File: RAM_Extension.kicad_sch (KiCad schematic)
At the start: 22 parts, among them J2 EXT, U1 LFE5U-85F-8BG381C, U4 IS66WVE4M16EBLL-70BLI

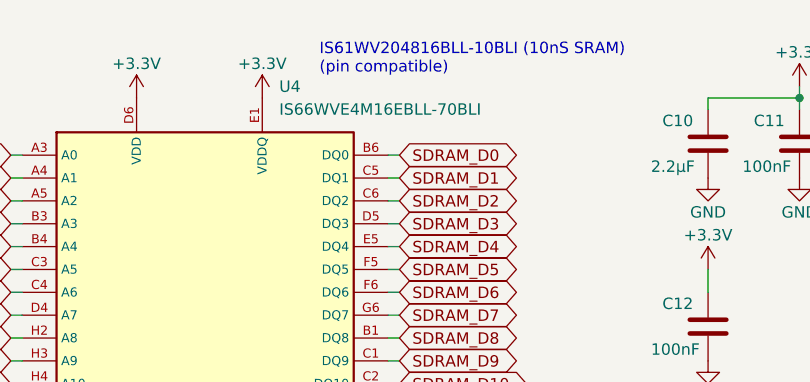
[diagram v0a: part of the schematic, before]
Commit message: Switched to project library
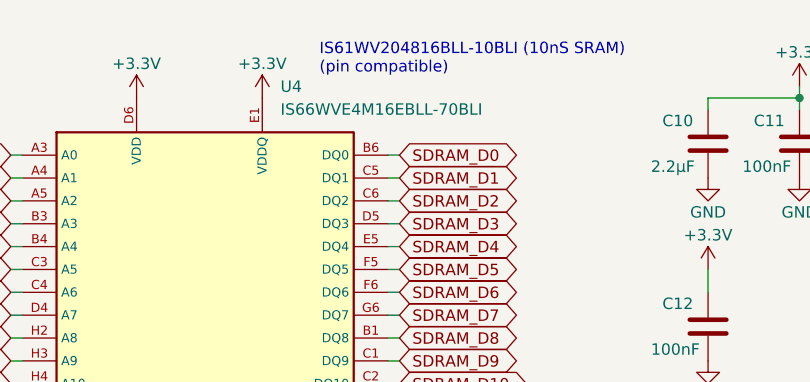
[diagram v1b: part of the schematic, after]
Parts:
- J2: footprint Gil:FTS-120-02-L-DV -> ECP5_RISCV:FTS-120-02-L-DV
- U1: footprint Gil:BGA-381_pitch0.8mm_dia0.4mm -> ECP5_RISCV:BGA-381_pitch0.8mm_dia0.4mm; symbol Gil:LFE5U-85F-6BG381x -> ECP5_RISCV:LFE5U-85F-6BG381x
- U4: footprint Gil:BGA48C75P8X6_800X600X120N -> ECP5_RISCV:BGA48C75P8X6_800X600X120N; symbol Gil:IS66WVE4M16E -> ECP5_RISCV:IS66WVE4M16E

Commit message: Changed the name of the project path to ECP5_BGA381_RISCV
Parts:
- J2: footprint ECP5_RISCV:FTS-120-02-L-DV -> ECP5_BGA381_RISCV:FTS-120-02-L-DV
- U1: footprint ECP5_RISCV:BGA-381_pitch0.8mm_dia0.4mm -> ECP5_BGA381_RISCV:BGA-381_pitch0.8mm_dia0.4mm; symbol ECP5_RISCV:LFE5U-85F-6BG381x -> ECP5_BGA381_RISCV:LFE5U-85F-6BG381x
- U4: footprint ECP5_RISCV:BGA48C75P8X6_800X600X120N -> ECP5_BGA381_RISCV:BGA48C75P8X6_800X600X120N; symbol ECP5_RISCV:IS66WVE4M16E -> ECP5_BGA381_RISCV:IS66WVE4M16E
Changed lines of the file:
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@@
 	)
 	(symbol
-		(lib_id "ECP5_RISCV:LFE5U-85F-6BG381x")
+		(lib_id "ECP5_BGA381_RISCV:LFE5U-85F-6BG381x")
 		(at 74.93 146.05 0)
 		(unit 4)
@@
 			)
 		)
-		(property "Footprint" "ECP5_RISCV:BGA-381_pitch0.8mm_dia0.4mm"
+		(property "Footprint" "ECP5_BGA381_RISCV:BGA-381_pitch0.8mm_dia0.4mm"
 			(at 71.12 -11.43 0)
 			(effects
@@
 	)
 	(symbol
-		(lib_id "ECP5_RISCV:LFE5U-85F-6BG381x")
+		(lib_id "ECP5_BGA381_RISCV:LFE5U-85F-6BG381x")
 		(at 114.3 148.59 0)
 		(unit 5)
@@
 			)
 		)
-		(property "Footprint" "ECP5_RISCV:BGA-381_pitch0.8mm_dia0.4mm"
+		(property "Footprint" "ECP5_BGA381_RISCV:BGA-381_pitch0.8mm_dia0.4mm"
 			(at 110.49 -8.89 0)
 			(effects
@@
 	)
 	(symbol
-		(lib_id "ECP5_RISCV:IS66WVE4M16E")
+		(lib_id "ECP5_BGA381_RISCV:IS66WVE4M16E")
 		(at 53.34 53.34 0)
 		(unit 1)
@@
 			)
 		)
-		(property "Footprint" "ECP5_RISCV:BGA48C75P8X6_800X600X120N"
+		(property "Footprint" "ECP5_BGA381_RISCV:BGA48C75P8X6_800X600X120N"
 			(at 53.34 53.34 0)
 			(effects
@@
 			)
 		)
-		(property "Footprint" "ECP5_RISCV:FTS-120-02-L-DV"
+		(property "Footprint" "ECP5_BGA381_RISCV:FTS-120-02-L-DV"
 			(at 153.67 60.96 0)
 			(effects
@@
 	)
 	(symbol
-		(lib_id "ECP5_RISCV:LFE5U-85F-6BG381x")
+		(lib_id "ECP5_BGA381_RISCV:LFE5U-85F-6BG381x")
 		(at 213.36 58.42 0)
 		(unit 7)
@@
 			)
 		)
-		(property "Footprint" "ECP5_RISCV:BGA-381_pitch0.8mm_dia0.4mm"
+		(property "Footprint" "ECP5_BGA381_RISCV:BGA-381_pitch0.8mm_dia0.4mm"
 			(at 209.55 -99.06 0)
 			(effects
@@
 	)
 	(symbol
-		(lib_id "ECP5_RISCV:LFE5U-85F-6BG381x")
+		(lib_id "ECP5_BGA381_RISCV:LFE5U-85F-6BG381x")
 		(at 260.35 58.42 0)
 		(unit 2)
@@
 			)
 		)
-		(property "Footprint" "ECP5_RISCV:BGA-381_pitch0.8mm_dia0.4mm"
+		(property "Footprint" "ECP5_BGA381_RISCV:BGA-381_pitch0.8mm_dia0.4mm"
 			(at 256.54 -99.06 0)
 			(effects
